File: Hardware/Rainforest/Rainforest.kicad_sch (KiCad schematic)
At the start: 41 parts, among them J1 Conn_01x08_Pin, J2 Conn_01x06_Pin, U1 STM32F401CCUx, U2 LY68L6400, Y1 32768 Hz, Y2 25MHz

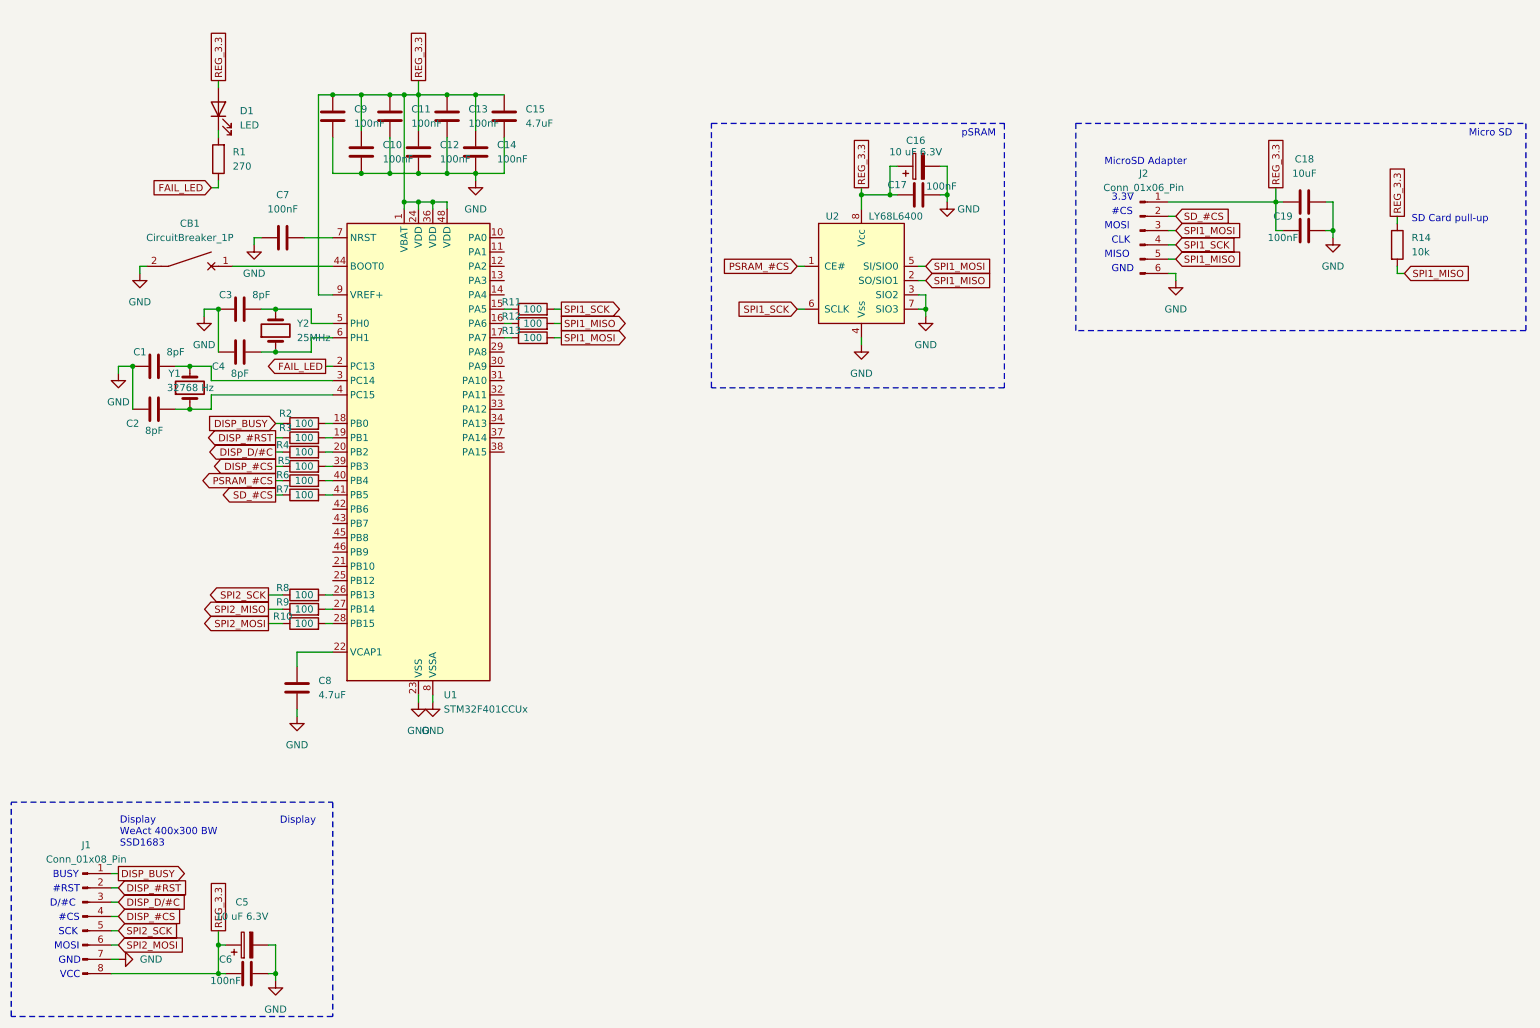
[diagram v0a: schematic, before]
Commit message: Added local BME-280 - temperature, humidity and pressure sensor
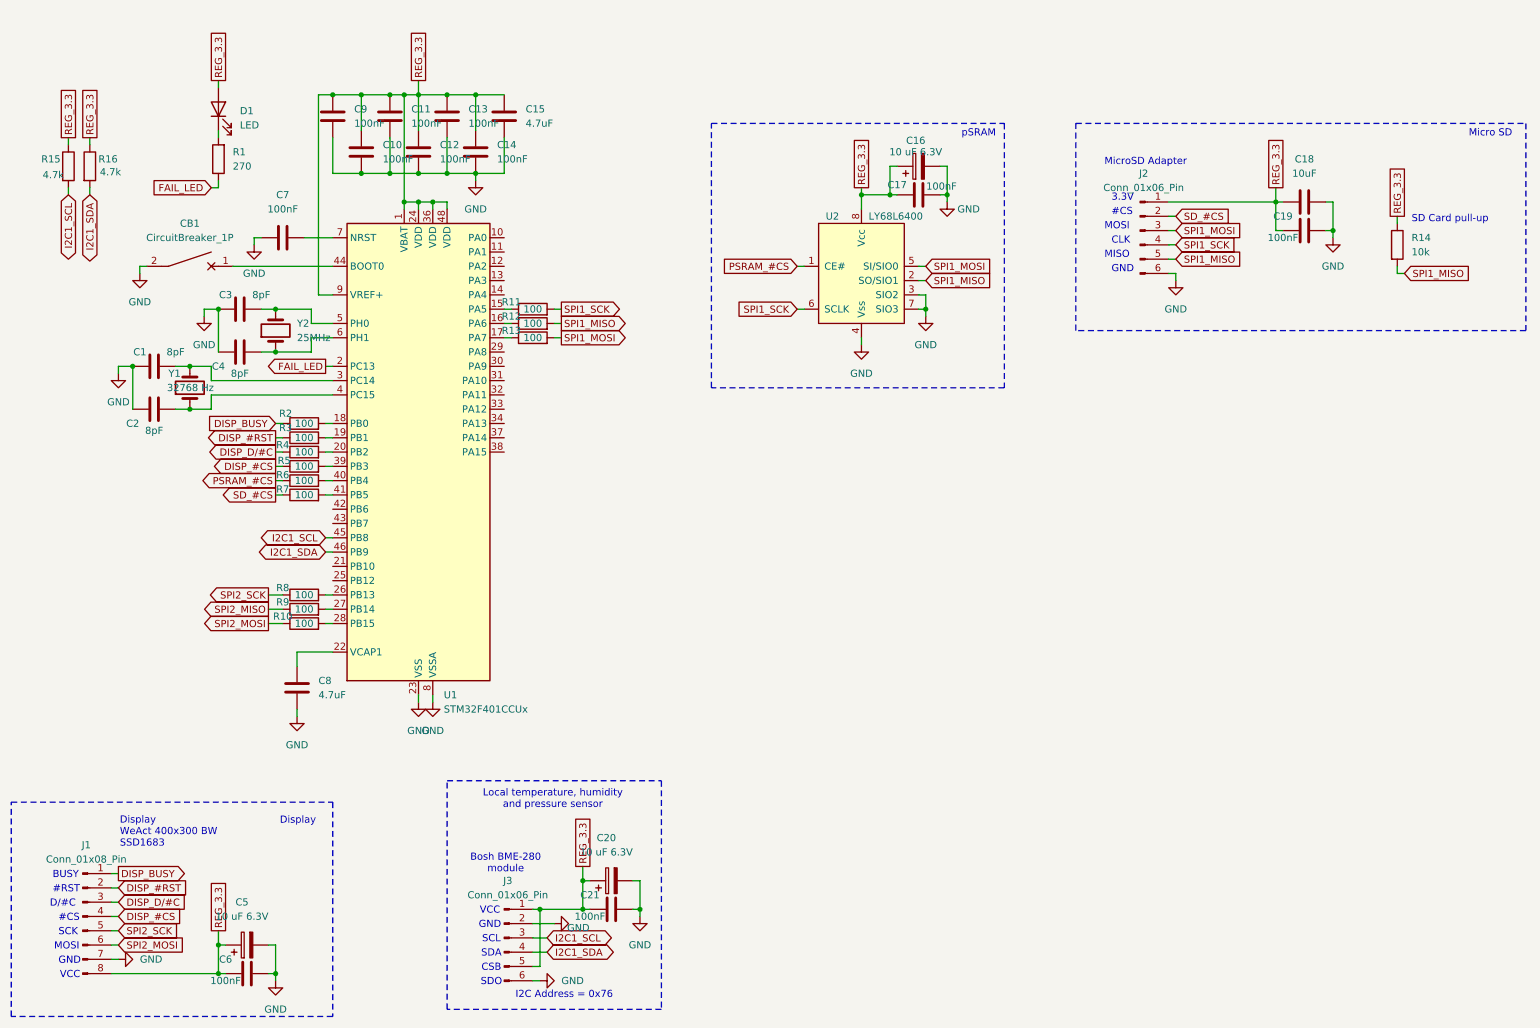
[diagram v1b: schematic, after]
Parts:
- added C20: 10 uF 6.3V, symbol Device:C_Polarized
- added C21: 100nF, symbol Device:C
- added J3: Conn_01x06_Pin, symbol Connector:Conn_01x06_Pin
- added R15, R16: 4.7k, symbol Device:R
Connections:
- net GND: now also C20.2, C21.2, J3.2 (Pin_2), J3.6 (Pin_6)
- net REG_3.3: now also C20.1, C21.1, J3.1 (Pin_1), J3.5 (Pin_5), R15.1, R16.1
- net I2C1_SCL: now reaches U1.45 (PB8)
- net I2C1_SCL: now also J3.3 (Pin_3), R15.2
- net I2C1_SDA: now reaches U1.46 (PB9)
- net I2C1_SDA: now also J3.4 (Pin_4), R16.2
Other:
- note added: "Bosh BME-280 module"
- note added: "CSB"
- note added: "I2C Address = 0x76"
- note added: "Local temperature, humidity and pressure sensor"
- note added: "SCL"
- note added: "SDA"
- note added: "SDO"

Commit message: Added Bluetooth (HC-06) adapter
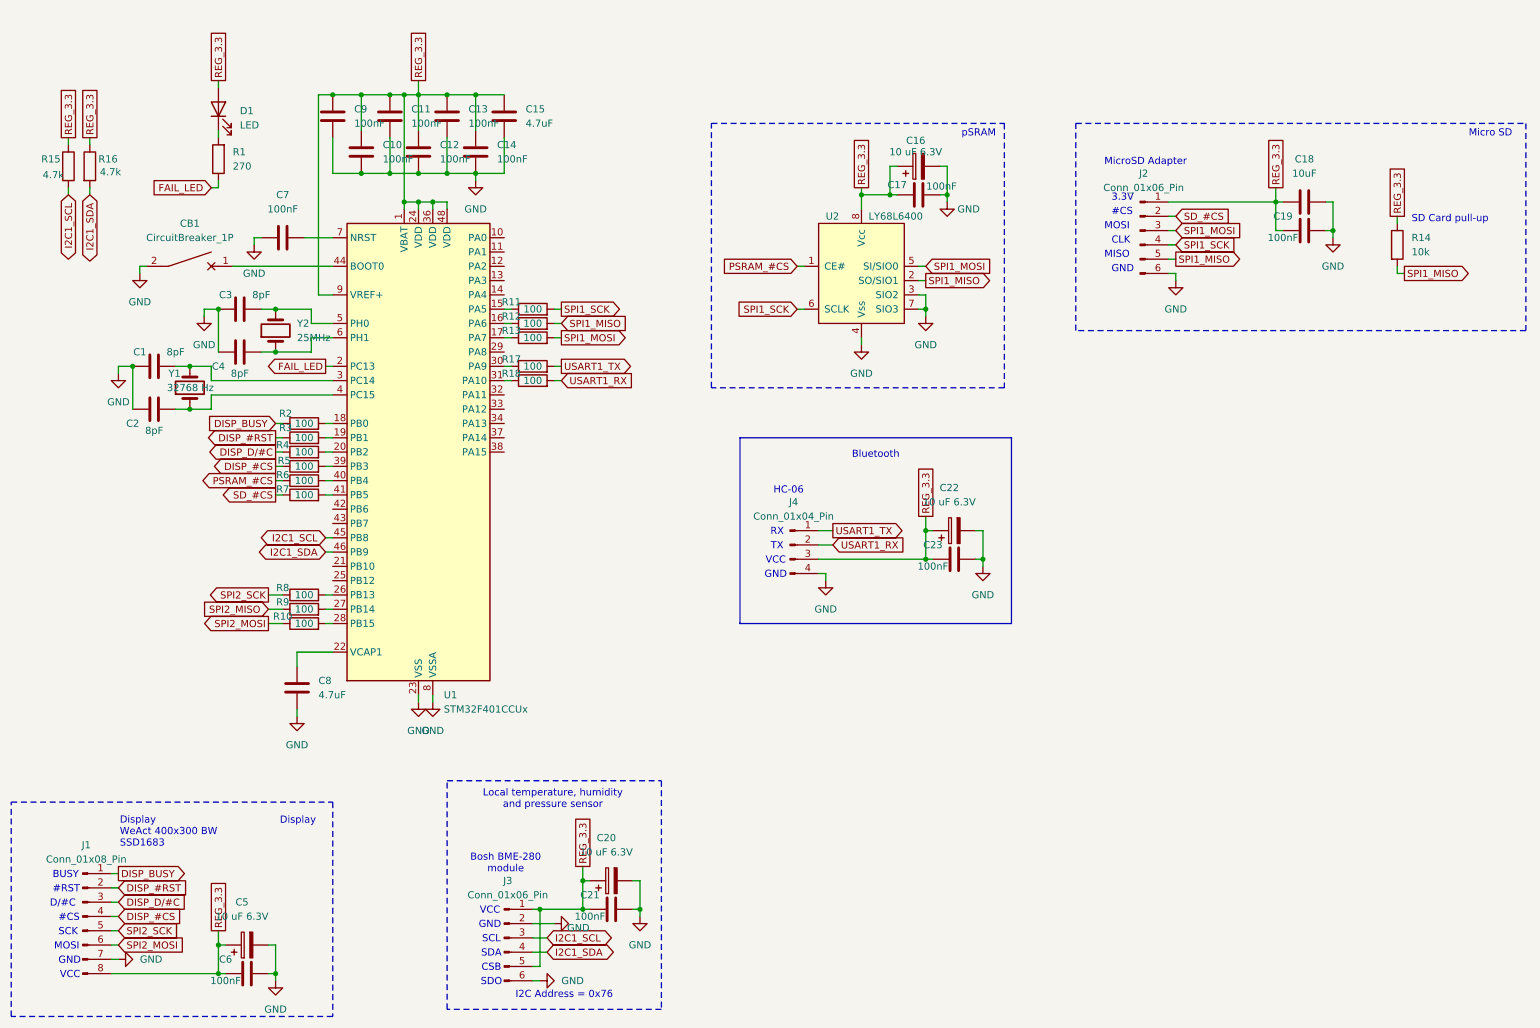
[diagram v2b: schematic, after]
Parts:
- added C22: 10 uF 6.3V, symbol Device:C_Polarized
- added C23: 100nF, symbol Device:C
- added J4: Conn_01x04_Pin, symbol Connector:Conn_01x04_Pin
- added R17, R18: 100, symbol Device:R
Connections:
- net GND: now also C22.2, C23.2, J4.4 (Pin_4)
- net REG_3.3: now also C22.1, C23.1, J4.3 (Pin_3)
- net at U1.30 (PA9): now also R17.1
- net at U1.31 (PA10): now also R18.1
- new net USART1_RX: J4.2 (Pin_2), R18.2
- new net USART1_TX: J4.1 (Pin_1), R17.2
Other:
- note added: "Bluetooth"
- note added: "HC-06"
- note added: "RX"
- note added: "TX"
